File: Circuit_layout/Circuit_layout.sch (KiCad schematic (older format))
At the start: 31 parts, among them SW1 SW_PUSH, U1 ADM6316, U15 TLP293, U17 MCP6004, U7 AT90CAN128-A, U9 TLP293, Y1 10MHz

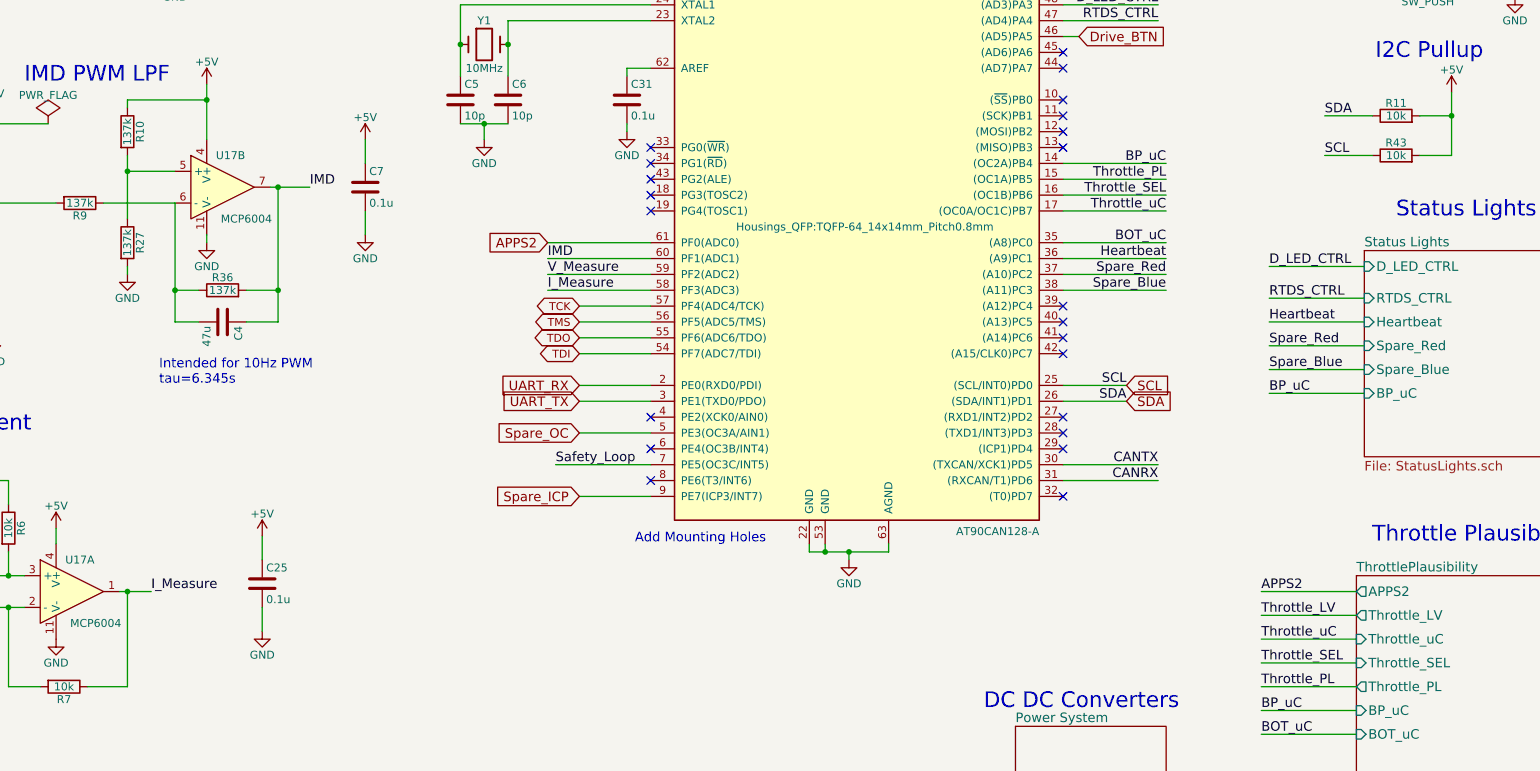
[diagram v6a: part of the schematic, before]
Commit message: added test pts
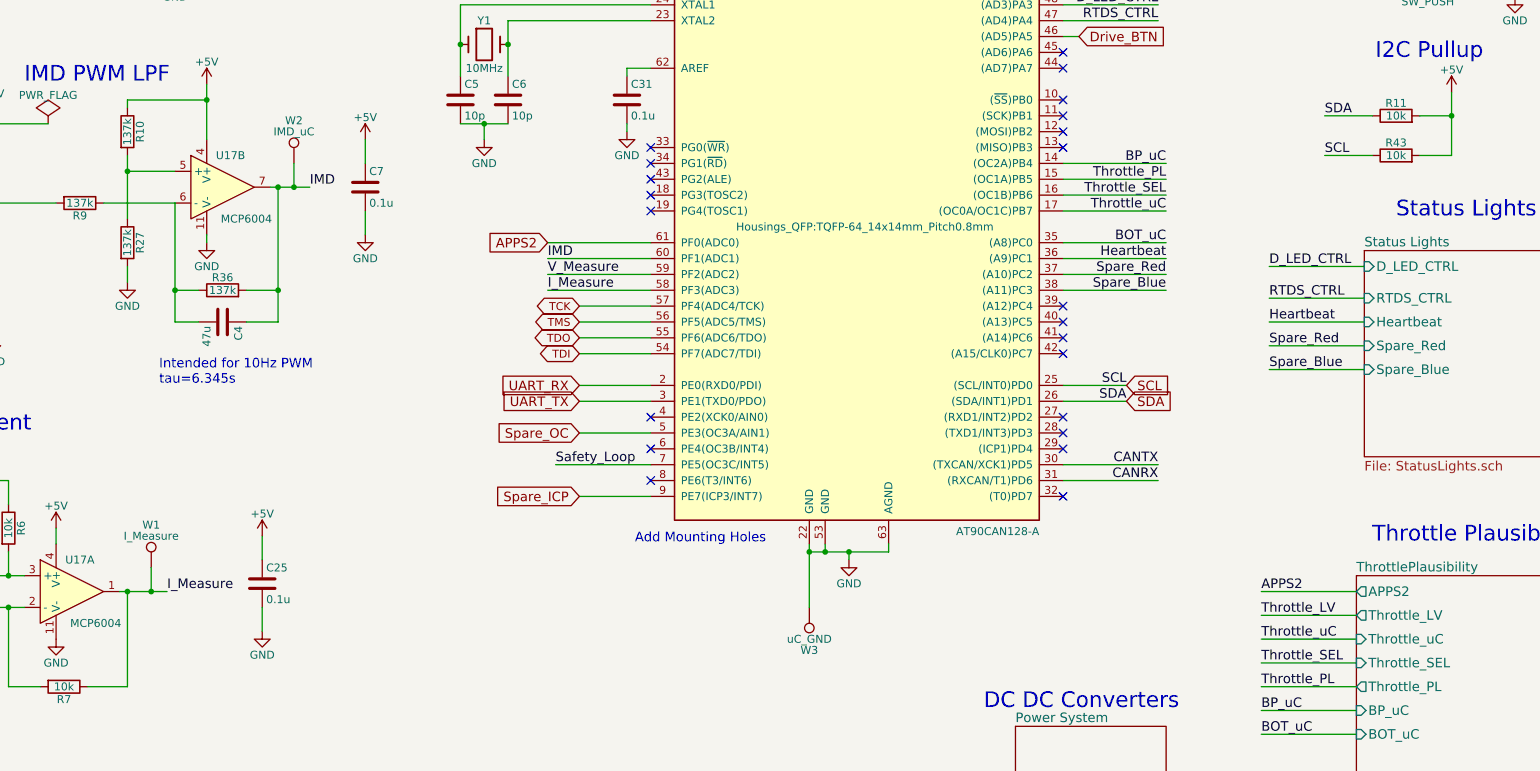
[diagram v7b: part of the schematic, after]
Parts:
- added W1: I_Measure, symbol TEST_1P
- added W2: IMD_uC, symbol TEST_1P
- added W3: uC_GND, symbol TEST_1P
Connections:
- net GND: now also W3.1
- net IMD: now also W2.1
- net I_Measure: now also W1.1
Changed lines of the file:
@@
 LIBS:xilinx
 LIBS:Zilog
+LIBS:pacman-main-cache
 LIBS:bss84
 LIBS:+10v
@@
 F2 "D_LED_CTRL" I L 11650 3200 60
 F3 "RTDS_CTRL" I L 11650 3400 60
-F4 "BP_uC" I L 11650 4000 60
 F5 "Heartbeat" I L 11650 3550 60
 F6 "Spare_Red" I L 11650 3700 60
@@
 Text Label 10350 1650 2    60   ~ 0
 RTDS_CTRL
-Text Label 4000 5250 0    60   ~ 0
+Text Label 4100 5250 0    60   ~ 0
 I_Measure
 $Sheet
@@
 Text Label 11000 6000 0    60   ~ 0
 BP_uC
-Text Label 11050 4000 0    60   ~ 0
-BP_uC
 Text Label 11050 3200 0    60   ~ 0
 D_LED_CTRL
@@
 $EndComp
 $Comp
-L GND #PWR013
-U 1 1 58BC4D85
-P 3850 3250
-F 0 "#PWR013" H 3850 3000 50  0001 C CNN
-F 1 "GND" H 3850 3100 50  0000 C CNN
-F 2 "" H 3850 3250 50  0000 C CNN
-F 3 "" H 3850 3250 50  0000 C CNN
-	1    3850 3250
-	1    0    0    -1
-$EndComp
-$Comp
 L C C7
 U 1 1 58BC98BF
@@
 $EndComp
 $Comp
-L +5V #PWR014
+L +5V #PWR013
 U 1 1 58BC98C5
 P 5350 2400
-F 0 "#PWR014" H 5350 2250 50  0001 C CNN
+F 0 "#PWR013" H 5350 2250 50  0001 C CNN
 F 1 "+5V" H 5350 2540 50  0000 C CNN
 F 2 "" H 5350 2400 50  0000 C CNN
@@
 $EndComp
 $Comp
-L GND #PWR015
+L GND #PWR014
 U 1 1 58BC98CB
 P 5350 3000
-F 0 "#PWR015" H 5350 2750 50  0001 C CNN
+F 0 "#PWR014" H 5350 2750 50  0001 C CNN
 F 1 "GND" H 5350 2850 50  0000 C CNN
 F 2 "" H 5350 3000 50  0000 C CNN
@@
 $EndComp
 $Comp
-L GND #PWR016
+L GND #PWR015
 U 1 1 58BB75AC
 P 4150 1350
-F 0 "#PWR016" H 4150 1100 50  0001 C CNN
+F 0 "#PWR015" H 4150 1100 50  0001 C CNN
 F 1 "GND" H 4150 1200 50  0000 C CNN
 F 2 "" H 4150 1350 50  0000 C CNN
@@
 $EndComp
 $Comp
-L GND #PWR017
+L GND #PWR016
 U 1 1 58BB7DFB
 P 3000 3650
-F 0 "#PWR017" H 3000 3400 50  0001 C CNN
+F 0 "#PWR016" H 3000 3400 50  0001 C CNN
 F 1 "GND" H 3000 3500 50  0000 C CNN
 F 2 "" H 3000 3650 50  0000 C CNN
@@
 $EndComp
 $Comp
-L +5V #PWR018
+L +5V #PWR017
 U 1 1 58BBF1E9
 P 3000 2250
-F 0 "#PWR018" H 3000 2100 50  0001 C CNN
+F 0 "#PWR017" H 3000 2100 50  0001 C CNN
 F 1 "+5V" H 3000 2390 50  0000 C CNN
 F 2 "" H 3000 2250 50  0000 C CNN
@@
 Isolator used to move \n24V PWM to 5V PWM for uC
 $Comp
-L PWR_FLAG #FLG019
+L PWR_FLAG #FLG018
 U 1 1 58BDECDC
 P 3350 2300
-F 0 "#FLG019" H 3350 2395 50  0001 C CNN
+F 0 "#FLG018" H 3350 2395 50  0001 C CNN
 F 1 "PWR_FLAG" H 3350 2480 50  0000 C CNN
 F 2 "" H 3350 2300 50  0000 C CNN
@@
 	7150 1250 6500 1250
 Wire Wire Line
-	8150 4950 8150 5000
+	8150 4950 8150 5350
 Wire Wire Line
 	8150 5000 8650 5000
@@
 	9750 1750 9850 1750
 Wire Wire Line
-	3800 5250 4000 5250
+	3800 5250 4100 5250
 Wire Wire Line
 	2000 5150 2650 5150
@@
 	4700 5050 4700 4900
 Wire Wire Line
-	11050 4000 11650 4000
-Wire Wire Line
 	11000 5250 11600 5250
 Wire Wire Line
@@
 Connection ~ 3850 2600
 Wire Wire Line
-	4350 3000 4350 3050
-Wire Wire Line
 	4150 2800 4150 3550
 Wire Wire Line
@@
 	3850 2150 4350 2150
 Connection ~ 4350 2150
-Wire Wire Line
-	3850 3200 3850 3250
 Wire Wire Line
 	3700 2800 4150 2800
@@
 Connection ~ 12200 2250
 $Comp
-L +5V #PWR020
+L +5V #PWR019
 U 1 1 58BE6C42
 P 12200 2100
-F 0 "#PWR020" H 12200 1950 50  0001 C CNN
+F 0 "#PWR019" H 12200 1950 50  0001 C CNN
 F 1 "+5V" H 12200 2240 50  0000 C CNN
 F 2 "" H 12200 2100 50  0000 C CNN
@@
 ~RESET_AVR
 $Comp
-L GND #PWR021
+L GND #PWR020
 U 1 1 58C057DD
 P 15950 2050
-F 0 "#PWR021" H 15950 1800 50  0001 C CNN
+F 0 "#PWR020" H 15950 1800 50  0001 C CNN
 F 1 "GND" H 15950 1900 50  0000 C CNN
 F 2 "" H 15950 2050 50  0000 C CNN
@@
 	17750 2200 17750 2350
 $Comp
-L GND #PWR022
+L GND #PWR021
 U 1 1 58C0B29F
 P 17750 2350
-F 0 "#PWR022" H 17750 2100 50  0001 C CNN
+F 0 "#PWR021" H 17750 2100 50  0001 C CNN
 F 1 "GND" H 17750 2200 50  0000 C CNN
 F 2 "" H 17750 2350 50  0000 C CNN
@@
 Connection ~ 17500 1850
 $Comp
-L +5V #PWR023
+L +5V #PWR022
 U 1 1 58C0C28E
 P 17500 1750
-F 0 "#PWR023" H 17500 1600 50  0001 C CNN
+F 0 "#PWR022" H 17500 1600 50  0001 C CNN
 F 1 "+5V" H 17500 1890 50  0000 C CNN
 F 2 "" H 17500 1750 50  0000 C CNN
@@
 	16000 2600 16000 2650
 $Comp
-L GND #PWR024
+L GND #PWR023
 U 1 1 58C0E11B
 P 16000 2650
-F 0 "#PWR024" H 16000 2400 50  0001 C CNN
+F 0 "#PWR023" H 16000 2400 50  0001 C CNN
 F 1 "GND" H 16000 2500 50  0000 C CNN
 F 2 "" H 16000 2650 50  0000 C CNN
@@
 	11400 1000 11400 950
 $Comp
-L +5V #PWR025
+L +5V #PWR024
 U 1 1 58C14221
 P 11400 950
-F 0 "#PWR025" H 11400 800 50  0001 C CNN
+F 0 "#PWR024" H 11400 800 50  0001 C CNN
 F 1 "+5V" H 11400 1090 50  0000 C CNN
 F 2 "" H 11400 950 50  0000 C CNN
@@
 ~RESET_AVR
 $Comp
-L GND #PWR026
+L GND #PWR025
 U 1 1 58BFFF85
 P 12600 1500
-F 0 "#PWR026" H 12600 1250 50  0001 C CNN
+F 0 "#PWR025" H 12600 1250 50  0001 C CNN
 F 1 "GND" H 12600 1350 50  0000 C CNN
 F 2 "" H 12600 1500 50  0000 C CNN
@@
 	0    1    1    0
 $EndComp
+$Comp
+L TEST_1P W3
+U 1 1 58C2BCC5
+P 8150 5350
+F 0 "W3" H 8150 5620 50  0000 C CNN
+F 1 "uC_GND" H 8150 5550 50  0000 C CNN
+F 2 "" H 8350 5350 50  0000 C CNN
+F 3 "" H 8350 5350 50  0000 C CNN
+	1    8150 5350
+	-1   0    0    1
+$EndComp
+Connection ~ 8150 5000
+$Comp
+L TEST_1P W2
+U 1 1 58C2CAF9
+P 4900 2550
+F 0 "W2" H 4900 2820 50  0000 C CNN
+F 1 "IMD_uC" H 4900 2750 50  0000 C CNN
+F 2 "" H 5100 2550 50  0000 C CNN
+F 3 "" H 5100 2550 50  0000 C CNN
+	1    4900 2550
+	1    0    0    -1
+$EndComp
+Wire Wire Line
+	4900 2550 4900 2700
+Connection ~ 4900 2700
+$Comp
+L TEST_1P W1
+U 1 1 58C2E496
+P 4000 5100
+F 0 "W1" H 4000 5370 50  0000 C CNN
+F 1 "I_Measure" H 4000 5300 50  0000 C CNN
+F 2 "" H 4200 5100 50  0000 C CNN
+F 3 "" H 4200 5100 50  0000 C CNN
+	1    4000 5100
+	1    0    0    -1
+$EndComp
+Wire Wire Line
+	4000 5100 4000 5250
+Connection ~ 4000 5250
+$Comp
+L GND #PWR026
+U 1 1 58C35653
+P 3850 3300
+F 0 "#PWR026" H 3850 3050 50  0001 C CNN
+F 1 "GND" H 3850 3150 50  0000 C CNN
+F 2 "" H 3850 3300 50  0000 C CNN
+F 3 "" H 3850 3300 50  0000 C CNN
+	1    3850 3300
+	1    0    0    -1
+$EndComp
+Wire Wire Line
+	3850 3200 3850 3300
+Wire Wire Line
+	4350 3000 4350 3050
 $EndSCHEMATC

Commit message: fixed switch, added pulldown resistor, added DPDT switch for extra ADCs
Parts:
- removed C13, C3: 0.1u, Capacitors_SMD:C_0805_HandSoldering, symbol C
- removed U1: ADM6316, symbol ADM6316
- added SW?: JS202011CQN, symbol JS202011CQN
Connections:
- net +5V: no longer R43.2
- net GND: now also R43.2
- net SCL: no longer R43.1
- net Throttle_SEL: now also R43.1
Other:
- note added: "NOTE: Add footprints to test points (already in lib)"
- note added: "No footprint"
- note added: "Throttle Select Pulldown"
- note removed: "Watchdog"
- moved on the sheet: C1, C2, C25, C31, C4, C5, C6, C7, R1, R10, R2, R27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
